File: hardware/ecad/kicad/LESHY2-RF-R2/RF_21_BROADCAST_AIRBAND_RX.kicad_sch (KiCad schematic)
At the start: 94 parts, among them J8 GCT RFPC-SMA31-FN-175-A, J9 GCT RFPC-SMA31-FN-175-A, U51 HMC544AETR, U52 PGA-103+, U53 SI5351A-B-GTR, U54 LT5560EDD#TRPBF, U55 WBC1-1TLC, U56 WBC16-1TLC, U57 HMC544AETR, U58 74LVC2G14GV,125, U59 Texas Instruments TPS22919DCKR, U60 Si4732-A10-GSR, U61 Seiko Epson Q13FC13500005, U62 Texas Instruments SN74LVC2G66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, U63 SN74LVC1G07DCKR, U64 Texas Instruments TPS22919DCKR, U65 Texas Instruments TPS3839K33D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, Y3 3225-27.00-10-10-10/A

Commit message: Verify factory-placeable Airband filter
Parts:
- removed C150: GCM1555C1H181FA16D, Capacitor_SMD:C_0402_1005Metric, symbol Leshy2_R2:murata_gcm1555c1h181fa16d
- removed C151: GJM1555C1H5R6BB01D, Capacitor_SMD:C_0402_1005Metric, symbol Leshy2_R2:murata_gjm1555c1h5r6bb01d
- removed C152: CQ0402BRNPO9BN6R2, Capacitor_SMD:C_0402_1005Metric, symbol Leshy2_R2:yageo_cq0402brnpo9bn6r2
- removed C153: CQ0402BRNPO9BN3R2, Capacitor_SMD:C_0402_1005Metric, symbol Leshy2_R2:yageo_cq0402brnpo9bn3r2
- removed C154: GJM1555C1H1R9WB01D, Capacitor_SMD:C_0402_1005Metric, symbol Leshy2_R2:murata_gjm1555c1h1r9wb01d
- removed C155: GJM1555C1H1R0WB01D, Capacitor_SMD:C_0402_1005Metric, symbol Leshy2_R2:murata_gjm1555c1h1r0wb01d
- removed C156: GJM1555C1H2R4WB01D, Capacitor_SMD:C_0402_1005Metric, symbol Leshy2_R2:murata_gjm1555c1h2r4wb01d
- removed C157: GJM1555C1H1R4WB01D, Capacitor_SMD:C_0402_1005Metric, symbol Leshy2_R2:murata_gjm1555c1h1r4wb01d
- removed C158: GJM1555C1H8R2BB01D, Capacitor_SMD:C_0402_1005Metric, symbol Leshy2_R2:murata_gjm1555c1h8r2bb01d
- removed C159: GJM1555C1H4R7BB01D, Capacitor_SMD:C_0402_1005Metric, symbol Leshy2_R2:murata_gjm1555c1h4r7bb01d
- removed L15: LQW15AN8N2G80D, Inductor_SMD:L_0402_1005Metric, symbol Leshy2_R2:murata_lqw15an8n2g80d
- removed L16: LQW2BASR22G00L, Inductor_SMD:L_0805_2012Metric, symbol Leshy2_R2:murata_lqw2basr22g00l
- removed L17: CS0805-R27J-S, Inductor_SMD:L_0805_2012Metric, symbol Leshy2_R2:chilisin_cs0805_r27j_s
- removed L18, L21, L23: LQW2BASR33G00L, Inductor_SMD:L_0805_2012Metric, symbol Leshy2_R2:murata_lqw2basr33g00l
- removed L19, L22, L24: LQW2UASR56F00L, Inductor_SMD:L_1008_2520Metric, symbol Leshy2_R2:murata_lqw2uasr56f00l
- removed L20: LQW2UAS1R0G00L, Inductor_SMD:L_1008_2520Metric, symbol Leshy2_R2:murata_lqw2uas1r0g00l
- added C150, C153: GCM1555C1H121FA16D, Capacitor_SMD:C_0402_1005Metric, symbol Leshy2_R2:murata_gcm1555c1h121fa16d
- added C151, C154: GJM1555C1H1R4WB01D, Capacitor_SMD:C_0402_1005Metric, symbol Leshy2_R2:murata_gjm1555c1h1r4wb01d
- added C152, C155: GCM1555C1H200FA16D, Capacitor_SMD:C_0402_1005Metric, symbol Leshy2_R2:murata_gcm1555c1h200fa16d
- added C156: GJM1555C1H5R7WB01D, Capacitor_SMD:C_0402_1005Metric, symbol Leshy2_R2:murata_gjm1555c1h5r7wb01d
- added C157: CC0402BRNPO9BN2R8, Capacitor_SMD:C_0402_1005Metric, symbol Leshy2_R2:yageo_cc0402brnpo9bn2r8
- added C158: GJM1555C1H5R8WB01D, Capacitor_SMD:C_0402_1005Metric, symbol Leshy2_R2:murata_gjm1555c1h5r8wb01d
- added L15, L16, L17, L18: LQW2BAS22NG00L, Inductor_SMD:L_0805_2012Metric, symbol Leshy2_R2:murata_lqw2bas22ng00l
- added L19, L22: LQW2BASR22G00L, Inductor_SMD:L_0805_2012Metric, symbol Leshy2_R2:murata_lqw2basr22g00l
- added L20, L23: LQW2BAS47NG00L, Inductor_SMD:L_0805_2012Metric, symbol Leshy2_R2:murata_lqw2bas47ng00l
- added L21: LQW2UASR56F00L, Inductor_SMD:L_1008_2520Metric, symbol Leshy2_R2:murata_lqw2uasr56f00l
- renumbered C160 to C159, C161 to C160, C162 to C161, C163 to C162, C164 to C163, C165 to C164, C166 to C165, C167 to C166, C168 to C167, C169 to C168, C170 to C169, C171 to C170, C172 to C171, C173 to C172, C174 to C173, C175 to C174, C176 to C175, C177 to C176, C178 to C177, C179 to C178, C180 to C179, C181 to C180, C182 to C181, C183 to C182, C184 to C183, C185 to C184, C186 to C185, C187 to C186, C188 to C187, C189 to C188, L25 to L24, L26 to L25, L27 to L26, L28 to L27, L29 to L28
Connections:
- net AIR_BPF_IN_RF: now also L19.1 (END_1)
- net AIR_BPF_OUT_RF: now also C158.2 (END_2)
- net POWER_GROUND: now also C150.2 (END_2), C151.2 (END_2), C152.2 (END_2), C153.2 (END_2), C154.2 (END_2), C155.2 (END_2), L15.2 (END_2), L16.2 (END_2), L17.2 (END_2), L18.2 (END_2)
- new net AIR_BPF_N1: C150.1 (END_1), C151.1 (END_1), C152.1 (END_1), C156.2 (END_2), L15.1 (END_1), L16.1 (END_1), L21.1 (END_1)
- new net AIR_BPF_N2: C153.1 (END_1), C154.1 (END_1), C155.1 (END_1), C157.2 (END_2), L17.1 (END_1), L18.1 (END_1), L22.1 (END_1)
- new net AIR_BPF_S1_LC: C156.1 (END_1), L20.2 (END_2)
- new net AIR_BPF_S1_L_MID: L19.2 (END_2), L20.1 (END_1)
- new net AIR_BPF_S2_LC: C157.1 (END_1), L21.2 (END_2)
- new net AIR_BPF_S3_LC: C158.1 (END_1), L23.2 (END_2)
- new net AIR_BPF_S3_L_MID: L22.2 (END_2), L23.1 (END_1)
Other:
- moved on the sheet: C159, C160, C161, C162, C163, C164, C165, C166, C167, C168, C169, C170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

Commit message: Complete current R2 schematic and sourcing revalidation
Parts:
- renumbered C150 to C155, C151 to C156, C152 to C157, C153 to C158, C154 to C159, C155 to C160, C156 to C161, C157 to C162, C158 to C163, C159 to C164, C160 to C165, C161 to C166, C162 to C167, C163 to C168, C164 to C169, C165 to C170, C166 to C171, C167 to C172, C168 to C173, C169 to C174, C170 to C175, C171 to C176, C172 to C177, C173 to C178, C174 to C179, C175 to C180, C176 to C181, C177 to C182, C178 to C183, C179 to C184, C180 to C185, C181 to C186, C182 to C187, C183 to C188, C184 to C189, C185 to C190, C186 to C191, C187 to C192, C188 to C193, L15 to L14, L16 to L15, L17 to L16, L18 to L17, L19 to L18, L20 to L19, L21 to L20, L22 to L21, L23 to L22, L24 to L23, L25 to L24, L26 to L25, L27 to L26, L28 to L27, R146 to R147, R147 to R148, R148 to R149, R149 to R150, R150 to R151, R151 to R152, R152 to R153, R153 to R154, R154 to R155, R155 to R156, R156 to R157, R157 to R158, R158 to R159, R159 to R160, R160 to R161, R161 to R162, R162 to R163, R163 to R164, R164 to R165, U51 to U52, U52 to U53, U53 to U54, U54 to U55, U55 to U56, U56 to U57, U57 to U58, U58 to U59, U59 to U60, U60 to U61, U61 to U62, U62 to U63, U63 to U64, U64 to U65, U65 to U66

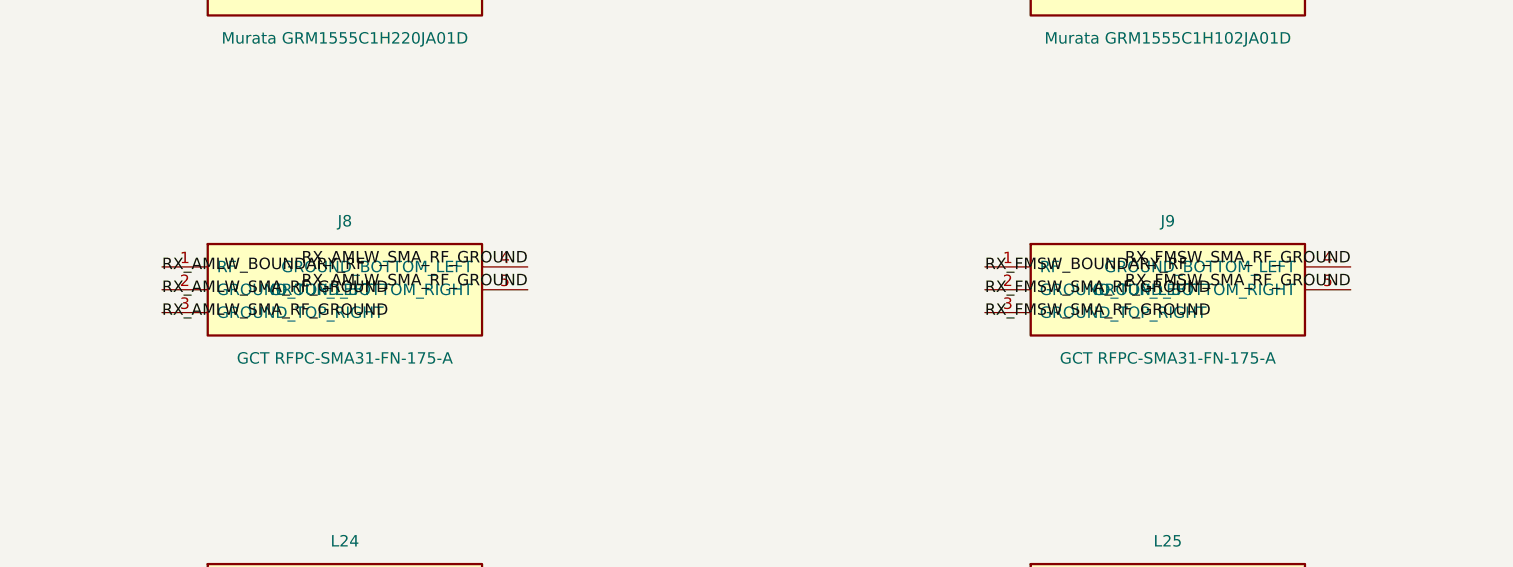
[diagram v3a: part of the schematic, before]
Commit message: Canonicalize physical ground anchors
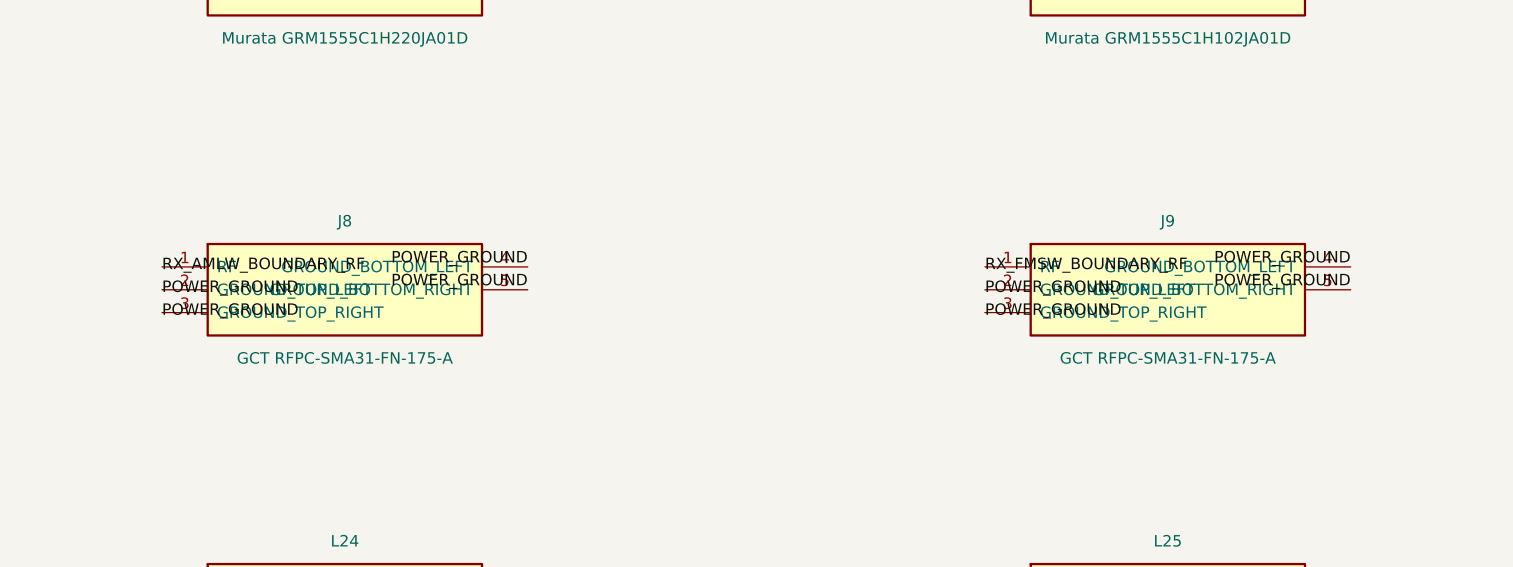
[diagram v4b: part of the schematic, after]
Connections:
- net RX_AMLW_SMA_RF_GROUND is gone; now on net POWER_GROUND: J8.2 (GROUND_TOP_LEFT), J8.3 (GROUND_TOP_RIGHT), J8.4 (GROUND_BOTTOM_LEFT), J8.5 (GROUND_BOTTOM_RIGHT)
- net RX_FMSW_SMA_RF_GROUND is gone; now on net POWER_GROUND: J9.2 (GROUND_TOP_LEFT), J9.3 (GROUND_TOP_RIGHT), J9.4 (GROUND_BOTTOM_LEFT), J9.5 (GROUND_BOTTOM_RIGHT)
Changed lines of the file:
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@@
 		(effects (font (size 1.27 1.27)))
 	)
-	(label "RX_AMLW_SMA_RF_GROUND"
+	(label "POWER_GROUND"
 		(at 492.76 158.75 0)
 		(effects (font (size 1.27 1.27)))
 	)
-	(label "RX_AMLW_SMA_RF_GROUND"
+	(label "POWER_GROUND"
 		(at 492.76 161.29 0)
 		(effects (font (size 1.27 1.27)))
 	)
-	(label "RX_AMLW_SMA_RF_GROUND"
+	(label "POWER_GROUND"
 		(at 533.40 156.21 180)
 		(effects (font (size 1.27 1.27)) (justify right bottom))
 	)
-	(label "RX_AMLW_SMA_RF_GROUND"
+	(label "POWER_GROUND"
 		(at 533.40 158.75 180)
 		(effects (font (size 1.27 1.27)) (justify right bottom))
@@
 		(effects (font (size 1.27 1.27)))
 	)
-	(label "RX_FMSW_SMA_RF_GROUND"
+	(label "POWER_GROUND"
 		(at 584.20 158.75 0)
 		(effects (font (size 1.27 1.27)))
 	)
-	(label "RX_FMSW_SMA_RF_GROUND"
+	(label "POWER_GROUND"
 		(at 584.20 161.29 0)
 		(effects (font (size 1.27 1.27)))
 	)
-	(label "RX_FMSW_SMA_RF_GROUND"
+	(label "POWER_GROUND"
 		(at 624.84 156.21 180)
 		(effects (font (size 1.27 1.27)) (justify right bottom))
 	)
-	(label "RX_FMSW_SMA_RF_GROUND"
+	(label "POWER_GROUND"
 		(at 624.84 158.75 180)
 		(effects (font (size 1.27 1.27)) (justify right bottom))

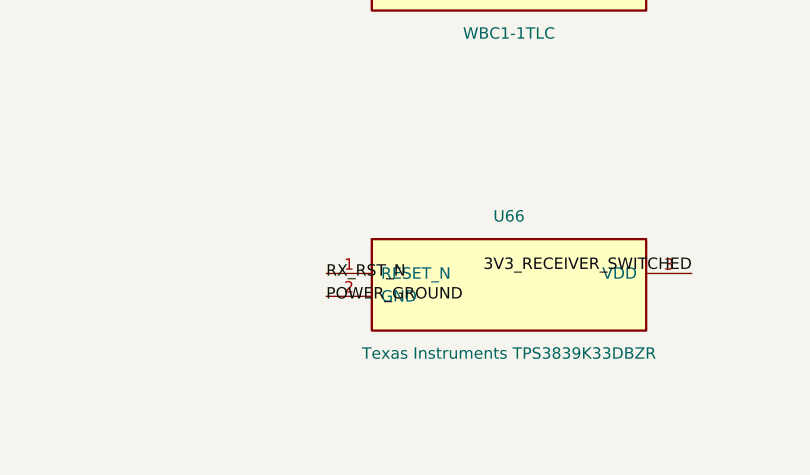
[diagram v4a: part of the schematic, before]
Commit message: Correct exact connector and protection geometry; expand electrical review
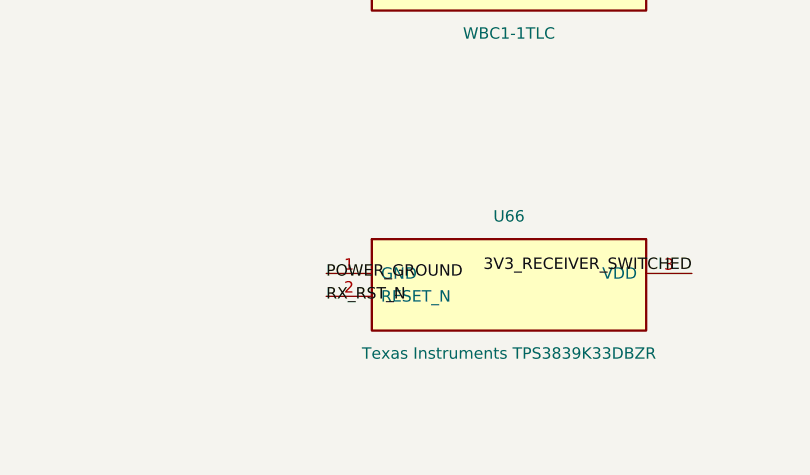
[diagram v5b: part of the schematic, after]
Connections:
- net POWER_GROUND: now also U66.1 (GND); no longer U66.2 (GND)
- net RX_RST_N: now also U66.2 (RESET_N); no longer U66.1 (RESET_N)
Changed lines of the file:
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@@
 		)
 	)
-	(label "RX_RST_N"
+	(label "POWER_GROUND"
 		(at 767.08 299.72 0)
 		(effects (font (size 1.27 1.27)))
 	)
-	(label "POWER_GROUND"
+	(label "RX_RST_N"
 		(at 767.08 302.26 0)
 		(effects (font (size 1.27 1.27)))

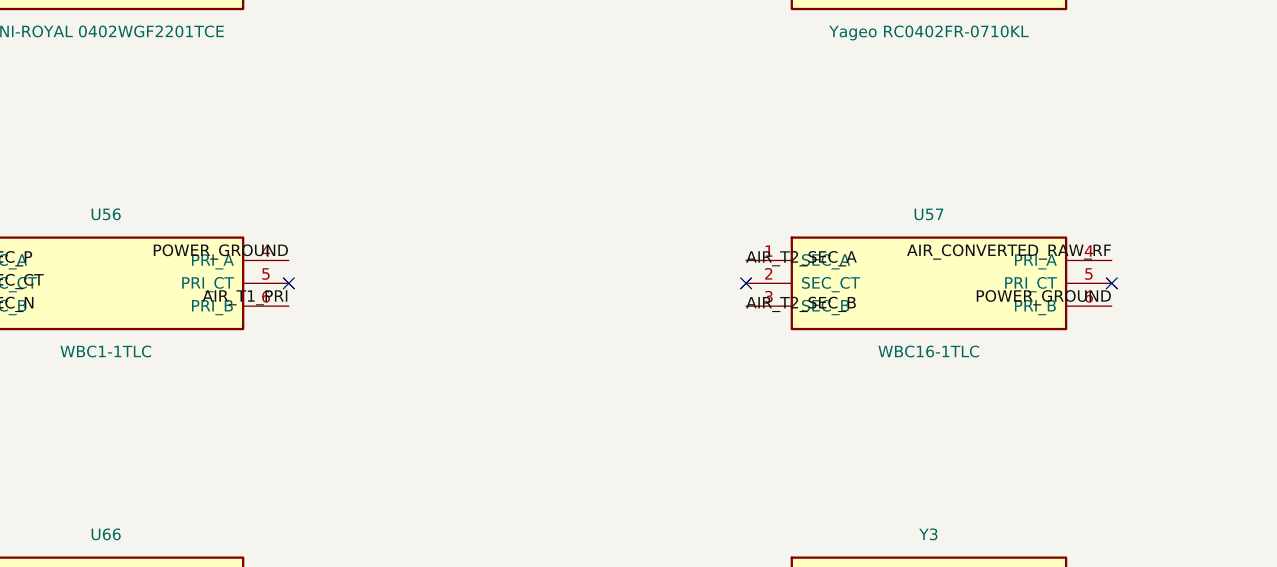
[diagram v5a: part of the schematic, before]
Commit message: Correct exact RF lands and reopen native power prerequisites
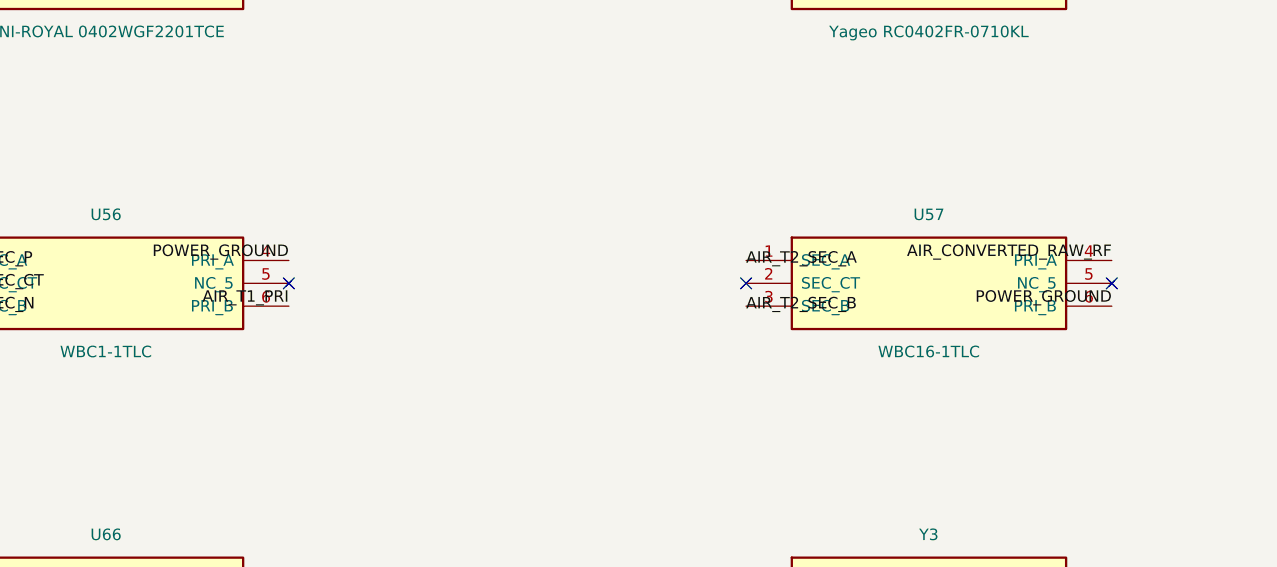
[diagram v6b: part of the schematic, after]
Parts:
- U56: footprint Leshy2_R2:Coilcraft_WBC_6P_4.45x4.19mm -> Leshy2_R2:WBC1-1TLC
- U57: footprint Leshy2_R2:Coilcraft_WBC_6P_4.45x4.19mm -> Leshy2_R2:WBC16-1TLC
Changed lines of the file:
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@@
 			(effects (font (size 1.27 1.27)))
 		)
-		(property "Footprint" "Leshy2_R2:Coilcraft_WBC_6P_4.45x4.19mm"
+		(property "Footprint" "Leshy2_R2:WBC1-1TLC"
 			(at 787.40 265.43 0)
 			(show_name no)
@@
 			(effects (font (size 1.27 1.27)))
 		)
-		(property "Footprint" "Leshy2_R2:Coilcraft_WBC_6P_4.45x4.19mm"
+		(property "Footprint" "Leshy2_R2:WBC16-1TLC"
 			(at 878.84 265.43 0)
 			(show_name no)
